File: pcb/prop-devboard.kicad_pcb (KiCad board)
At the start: 4 copper layers, 50.8 x 22.9 mm, 43 parts, among them CN1 STDC14, CN2 SM04B-SRSS-TB (LF)(SN), CN3 ZX-PH2.0-WT2P, CN4 SM04B-SRSS-TB (LF)(SN), J1 Conn_01x12, J2 Conn_01x16, J3 GT-USB-7010ASV, Q1 DMG3415U-7, SW1 SW_Push, U1 STM32G0B1CBT6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

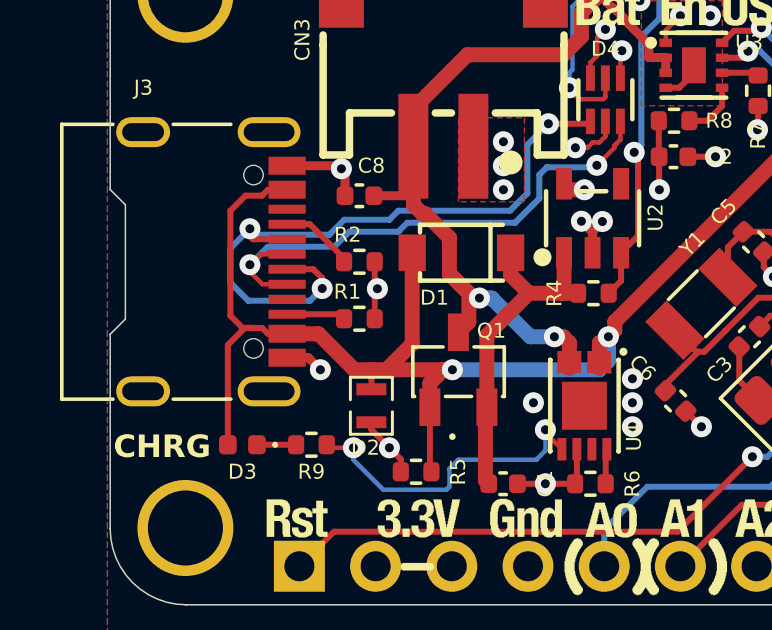
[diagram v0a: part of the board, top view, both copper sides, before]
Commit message: Improved track connection to USB VBUS pads (was too thin)
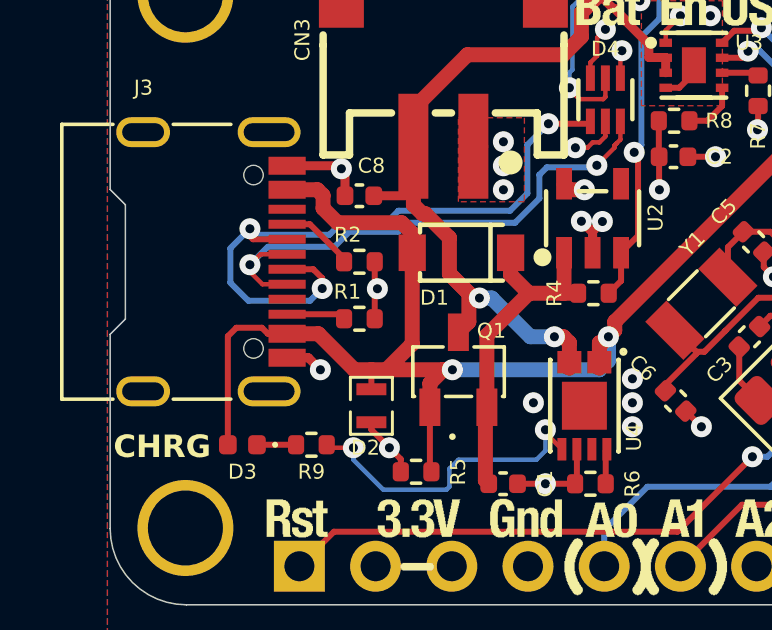
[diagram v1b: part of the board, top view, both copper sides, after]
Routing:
- net VBUS: track 61.9 -> 60.9 mm
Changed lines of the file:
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@@
-	)
-	(segment
-		(start 105.154151 93.104)
-		(end 105 93.104)
-		(width 0.2)
-		(layer "F.Cu")
-		(net 58)
 	)
 	(segment
@@
 	)
 	(segment
-		(start 104.015 97)
-		(end 104.015 93.674849)
-		(width 0.2)
-		(layer "F.Cu")
-		(net 58)
-	)
-	(segment
 		(start 117.876 82.074)
 		(end 119.826 82.074)
@@
 	)
 	(segment
+		(start 104.015 93.385)
+		(end 104.3 93.1)
+		(width 0.2)
+		(layer "F.Cu")
+		(net 58)
+	)
+	(segment
 		(start 110.8 97.9)
 		(end 110.8 97.8)
@@
 	)
 	(segment
-		(start 105.154151 88.696)
-		(end 104.604 88.696)
-		(width 0.2)
+		(start 105.350151 93.3)
+		(end 105.99 93.3)
+		(width 0.2)
+		(layer "F.Cu")
+		(net 58)
+	)
+	(segment
+		(start 107.670318 89.6)
+		(end 109.808636 89.6)
+		(width 0.5)
 		(layer "F.Cu")
 		(net 58)
@@
 	)
 	(segment
-		(start 105.794 93.104)
-		(end 105.99 93.3)
-		(width 0.2)
-		(layer "F.Cu")
-		(net 58)
-	)
-	(segment
 		(start 115.449998 85.2)
 		(end 115.449998 85.149998)
@@
 	)
 	(segment
-		(start 104.1 92.7)
-		(end 104.504 93.104)
-		(width 0.2)
-		(layer "F.Cu")
-		(net 58)
-	)
-	(segment
 		(start 110.16 93.64)
 		(end 110.16 90.6)
@@
 	)
 	(segment
-		(start 105.350151 93.3)
-		(end 105.154151 93.104)
-		(width 0.2)
-		(layer "F.Cu")
-		(net 58)
-	)
-	(segment
-		(start 105.350151 88.5)
-		(end 105.154151 88.696)
-		(width 0.2)
-		(layer "F.Cu")
-		(net 58)
-	)
-	(segment
-		(start 104.504 93.104)
-		(end 104.8 93.104)
-		(width 0.2)
-		(layer "F.Cu")
-		(net 58)
-	)
-	(segment
-		(start 104.585849 93.104)
-		(end 104.8 93.104)
-		(width 0.2)
-		(layer "F.Cu")
-		(net 58)
-	)
-	(segment
-		(start 104.8 93.104)
-		(end 105 93.104)
-		(width 0.2)
-		(layer "F.Cu")
-		(net 58)
-	)
-	(segment
 		(start 116.526 85.481)
 		(end 115.730998 85.481)
@@
 	)
 	(segment
+		(start 105.99 88.5)
+		(end 107 88.5)
+		(width 0.5)
+		(layer "F.Cu")
+		(net 58)
+	)
+	(segment
+		(start 105.150151 93.1)
+		(end 105.350151 93.3)
+		(width 0.2)
+		(layer "F.Cu")
+		(net 58)
+	)
+	(segment
 		(start 116.7 93.4)
 		(end 116.912472 93.187528)
@@
 	)
 	(segment
+		(start 109.808636 89.6)
+		(end 110.16 89.951364)
+		(width 0.5)
+		(layer "F.Cu")
+		(net 58)
+	)
+	(segment
 		(start 116.6 84.78)
 		(end 116.6 85.407)
@@
 	)
 	(segment
-		(start 105.99 93.3)
-		(end 105.350151 93.3)
-		(width 0.2)
+		(start 110.16 89.951364)
+		(end 110.16 90.6)
+		(width 0.5)
+		(layer "F.Cu")
+		(net 58)
+	)
+	(segment
+		(start 107 88.5)
+		(end 107.189 88.689)
+		(width 0.5)
 		(layer "F.Cu")
 		(net 58)
@@
 	)
 	(segment
-		(start 104.604 88.696)
-		(end 104.1 89.2)
-		(width 0.2)
+		(start 107.189 89.118682)
+		(end 107.670318 89.6)
+		(width 0.5)
+		(layer "F.Cu")
+		(net 58)
+	)
+	(segment
+		(start 107.189 88.689)
+		(end 107.189 89.118682)
+		(width 0.5)
 		(layer "F.Cu")
 		(net 58)
@@
 	)
 	(segment
+		(start 104.3 93.1)
+		(end 105.150151 93.1)
+		(width 0.2)
+		(layer "F.Cu")
+		(net 58)
+	)
+	(segment
 		(start 121.175 80.725)
 		(end 121.655 80.725)
@@
 	)
 	(segment
-		(start 104.1 89.2)
-		(end 104.1 92.7)
-		(width 0.2)
-		(layer "F.Cu")
-		(net 58)
-	)
-	(segment
 		(start 108.8 94.5)
 		(end 108.232786 94.5)
@@
 	)
 	(segment
-		(start 105.99 88.5)
-		(end 105.350151 88.5)
-		(width 0.2)
-		(layer "F.Cu")
-		(net 58)
-	)
-	(segment
 		(start 116.7 93.4)
 		(end 116.5 93.6)
@@
 	)
 	(segment
-		(start 104.015 93.674849)
-		(end 104.585849 93.104)
-		(width 0.2)
-		(layer "F.Cu")
-		(net 58)
-	)
-	(segment
 		(start 116.912472 93.187528)
 		(end 116.912472 92.9)
@@
 		(layer "F.Cu")
 		(net 58)
+	)
+	(segment
+		(start 104.015 97)
+		(end 104.015 93.385)
+		(width 0.2)
+		(layer "F.Cu")
+		(net 58)

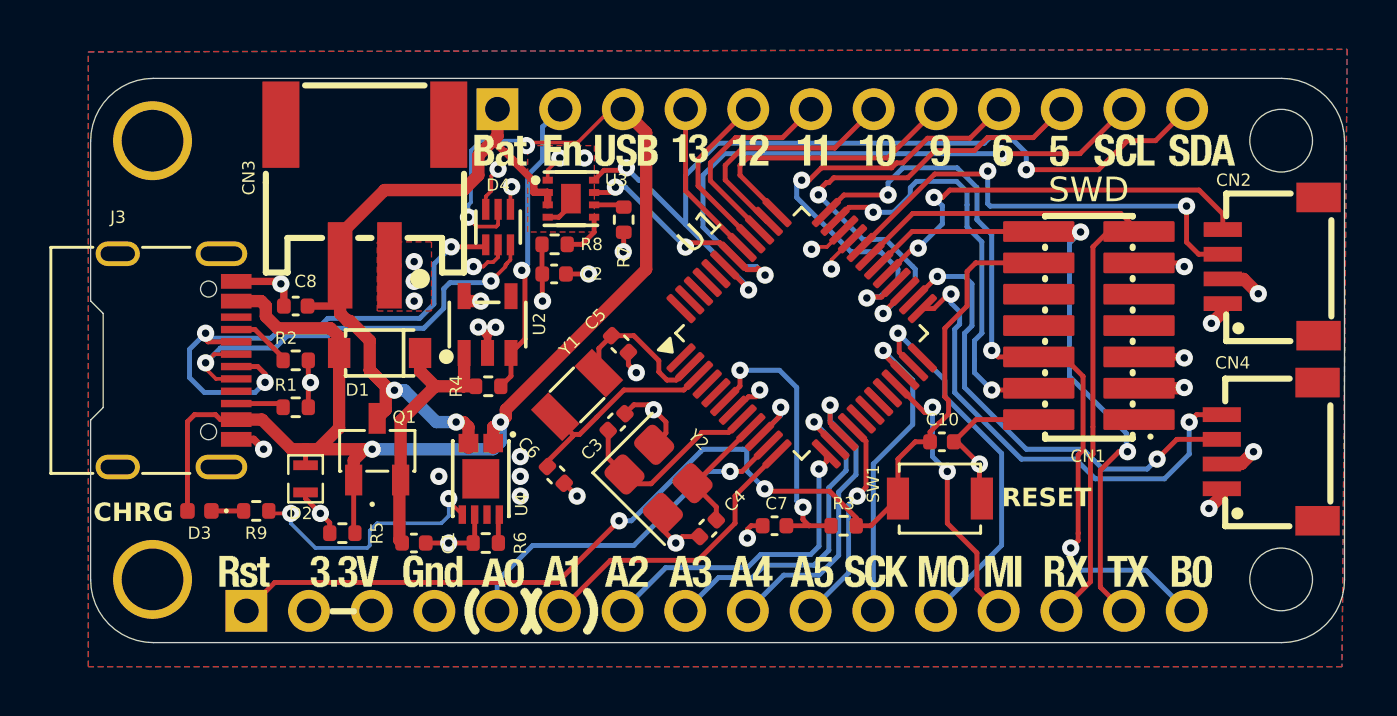
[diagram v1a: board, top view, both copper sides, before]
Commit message: Added power and status LEDs to the design
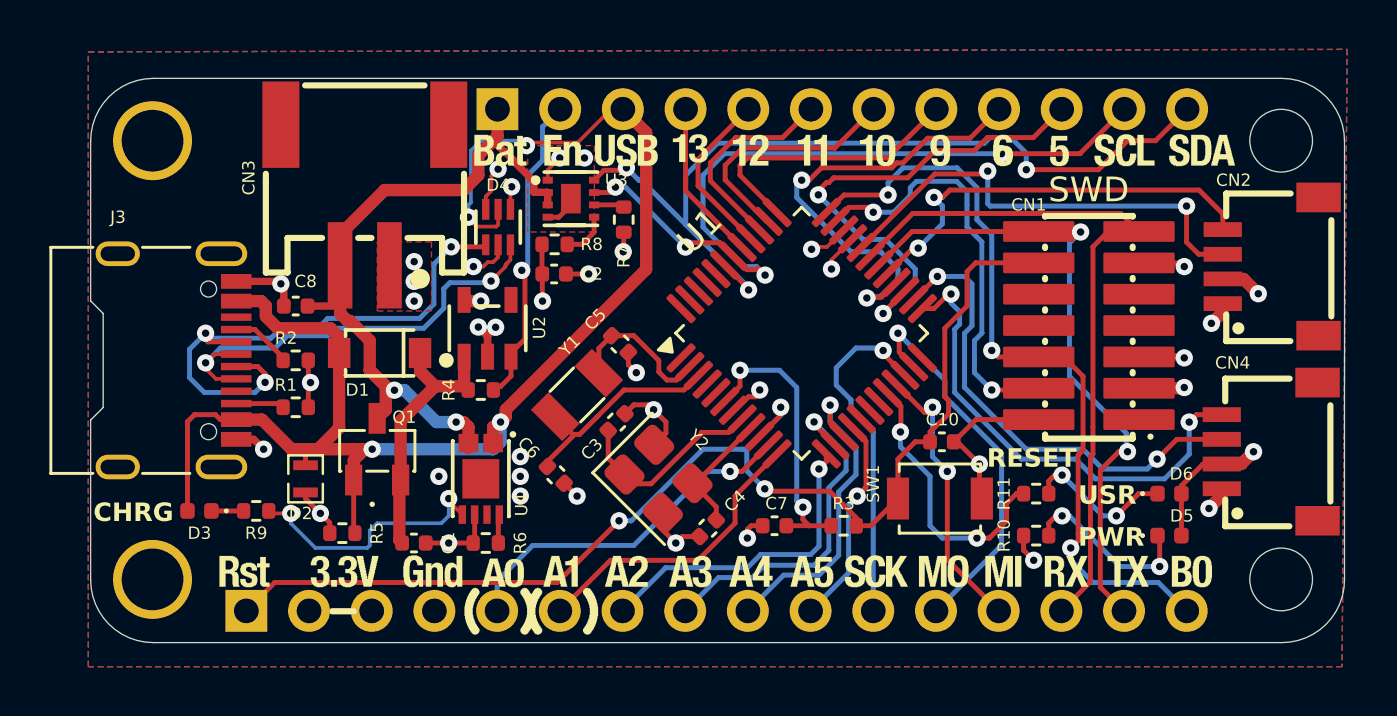
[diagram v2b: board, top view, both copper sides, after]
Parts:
- added D5: RED, LED_SMD:LED_0402_1005Metric, F.Cu at (143.8, 98.0)
- added D6: YELLOW GREEN, LED_SMD:LED_0402_1005Metric, F.Cu at (143.8, 96.3)
- added R10: 5K1, Resistor_SMD:R_0402_1005Metric, F.Cu at (138.4, 98.0)
- added R11: 5K1, Resistor_SMD:R_0402_1005Metric, F.Cu at (138.4, 96.3)
- added REF**: OSHW-Logo2_7.3x6mm_SilkScreen, Symbol:OSHW-Logo2_7.3x6mm_SilkScreen, B.Cu at (111.0, 93.7)
- moved R4 0.34 mm to (115.9, 92.1)
- moved U2 0.15 mm to (116.2, 89.6)
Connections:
- U1 pad 20: unconnected-(U1-PB1-Pad20) -> LED_USR
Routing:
- net LED_USR: track 0.00 -> 11.3 mm, vias 0 -> 2
- net Net-(D5-K): track 0.00 -> 7.26 mm, vias 0 -> 2
- net Net-(D6-K): track 0.00 -> 6.07 mm, vias 0 -> 2
- net +3V3: track 76.6 -> 80.6 mm
- net GND: track 43.6 -> 44.7 mm, vias 30 -> 31
- net SPI_SCK: track 13.1 -> 14.1 mm
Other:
- board text added: "Designed by: ~dogfault"
- board text added: "Feather STM32G0B1 Community Feather"
- board text added: "PWR"
- board text added: "USR"

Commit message: Added revision number
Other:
- board text added: "Feather STM32G0B1 Rev. A Community Feather"
- board text removed: "Feather STM32G0B1 Community Feather"
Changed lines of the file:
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@@
 		)
 	)
-	(gr_text "Feather STM32G0B1\nCommunity Feather"
+	(gr_text "Feather STM32G0B1 Rev. A\nCommunity Feather"
 		(at 147.8 89.1 0)
 		(layer "B.SilkS")
